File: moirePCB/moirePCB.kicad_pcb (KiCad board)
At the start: 4 copper layers, 38 x 215.8 mm, 57 parts, among them J1 USB_C_Receptacle, U1 ESP32-PICO-D4, U10 TLV73333PDBV, U2 BQ25504, U3 TLV73333PDBV, U4 RFM95W-915S2, U5 CH340E, U6 TLC555xD, U7 HDC1080, U8 AP2281-1WG-7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

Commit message: Daughter Board changes from meeting
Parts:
- removed ACC_RAIL_JP1, BATTMEASURE_JP1, LDO_JP1, TEMP_SCL_JP1, TEMP_SDA_JP1, VBAT_OK1: SolderJumper_2_Bridged, Jumper:SolderJumper-2_P1.3mm_Bridged_RoundedPad1.0x1.5mm
- removed AE1: T1-915M Antenna, Connector_PinHeader_2.54mm:PinHeader_1x01_P2.54mm_Vertical
- removed BOOT1, EN1: SW_Push, Button_Switch_SMD:SW_Push_1P1T_XKB_TS-1187A
- removed BT1: Battery_Cell, Connector_JST:JST_PH_S2B-PH-K_1x02_P2.00mm_Horizontal
- removed C1: .1u, Capacitor_SMD:C_0805_2012Metric
- removed C2, C6: 12pF/50V, Capacitor_SMD:C_0805_2012Metric
- removed C3: .01uF, Capacitor_SMD:C_0805_2012Metric
- removed C5: 10u, Capacitor_SMD:C_0805_2012Metric
- removed C7: 100nF, Capacitor_SMD:C_0805_2012Metric
- removed C_FLTR1: .1uF, Capacitor_SMD:C_0805_2012Metric
- removed C_HVR1, C_STOR1: 4.7uF, Capacitor_SMD:C_0805_2012Metric
- removed LDR1: R_Photo 50k-100k, Connector_PinHeader_2.54mm:PinHeader_1x02_P2.54mm_Horizontal
- removed L_BST1: 22uH, Inductor_SMD:L_0805_2012Metric
- removed R10: 360k, Resistor_SMD:R_0805_2012Metric
- removed R4: 270k, Resistor_SMD:R_0805_2012Metric
- removed R6: 5.1k, Resistor_SMD:R_0805_2012Metric
- removed R7: 820k, Resistor_SMD:R_0805_2012Metric
- removed REF** (x2): MountingHole_3.2mm_M3_DIN965_Pad, MountingHole:MountingHole_3.2mm_M3_DIN965_Pad
- removed R_OC+10: 10M, Resistor_SMD:R_0805_2012Metric
- removed R_OC_1: 5.76M, Resistor_SMD:R_0805_2012Metric
- removed R_OC_2: 4.12M, Resistor_SMD:R_0805_2012Metric
- removed R_OK_1: 3.57M, Resistor_SMD:R_0805_2012Metric
- removed R_OK_2, R_UV_2: 6.19M, Resistor_SMD:R_0805_2012Metric
- removed R_OK_3: .143M, Resistor_SMD:R_0805_2012Metric
- removed R_OV_1: 4.42M, Resistor_SMD:R_0805_2012Metric
- removed R_OV_2: 5.36M, Resistor_SMD:R_0805_2012Metric
- removed R_UV_1: 3.74M, Resistor_SMD:R_0805_2012Metric
- removed SC1: Solar_Cell, Connector_PinHeader_2.54mm:PinHeader_1x02_P2.54mm_Horizontal
- removed U1: ESP32-PICO-D4, Package_DFN_QFN:QFN-48-1EP_7x7mm_P0.5mm_EP5.3x5.3mm
- removed U10, U3: TLV73333PDBV, Package_TO_SOT_SMD:SOT-23-5
- removed U2: BQ25504, Package_DFN_QFN:VQFN-16-1EP_3x3mm_P0.5mm_EP1.68x1.68mm
- removed U4: RFM95W-915S2, RF_Module:HOPERF_RFM9XW_SMD
- removed U5: CH340E, Package_SO:MSOP-10_3x3mm_P0.5mm
- removed U8, U9: AP2281-1WG-7, Package_TO_SOT_SMD:SOT-23-6
- removed USB//OFF1, USB//SOLAR1: SW_DPDT_x2, Button_Switch_SMD:SW_SPDT_PCM12
- removed Y2: 32.768kHz, Crystal:Crystal_SMD_MicroCrystal_CM9V-T1A-2Pin_1.6x1.0mm
- added J2: Conn_01x13, Connector_PinHeader_2.54mm:PinHeader_1x13_P2.54mm_Vertical, F.Cu at (70.9, 72.1)
- J1: value USB_C_Receptacle -> Conn_01x13; footprint Connector_USB:USB_C_Receptacle_HRO_TYPE-C-31-M-12 -> Connector_PinHeader_2.54mm:PinHeader_1x13_P2.54mm_Vertical
- moved U7 60.8 mm to (70.6, 109.7)
- moved J1 45.1 mm to (38.5, 72.2), turned to 0 degrees
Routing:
- net VCC: track 141.9 -> 0.00 mm, vias 7 -> 0
- net A_VCC: track 164.7 -> 48.8 mm
- net Net-(BT1-+): track 107.4 -> 0.00 mm, vias 2 -> 0
- net Net-(SC1-+): track 105.1 -> 0.00 mm, vias 2 -> 0
- net FREQOUT: track 97.2 -> 0.00 mm, vias 2 -> 0
- net /USB5V: track 84.1 -> 0.00 mm, vias 3 -> 0
- net ACCESSORY_SW: track 82.3 -> 0.00 mm, vias 3 -> 0
- net GND: track 354.2 -> 278.6 mm, vias 27 -> 8
- net LDR_MEASURE: track 40.4 -> 0.00 mm, vias 2 -> 0
- net Net-(U2-VIN_DC): track 39.8 -> 0.00 mm, vias 2 -> 0
- net /GPIO_21: track 39.3 -> 0.00 mm
- net Net-(AE1-A): track 35.8 -> 0.00 mm, vias 1 -> 0
- net Net-(U2-VRDIV): track 35.1 -> 0.00 mm, vias 2 -> 0
- net Net-(J2-Pin_5): track 34.7 -> 0.00 mm
- net /D+: track 32.1 -> 0.00 mm
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- removed copper zone on In2.Cu, net GND
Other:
- copper layers 4 -> 2

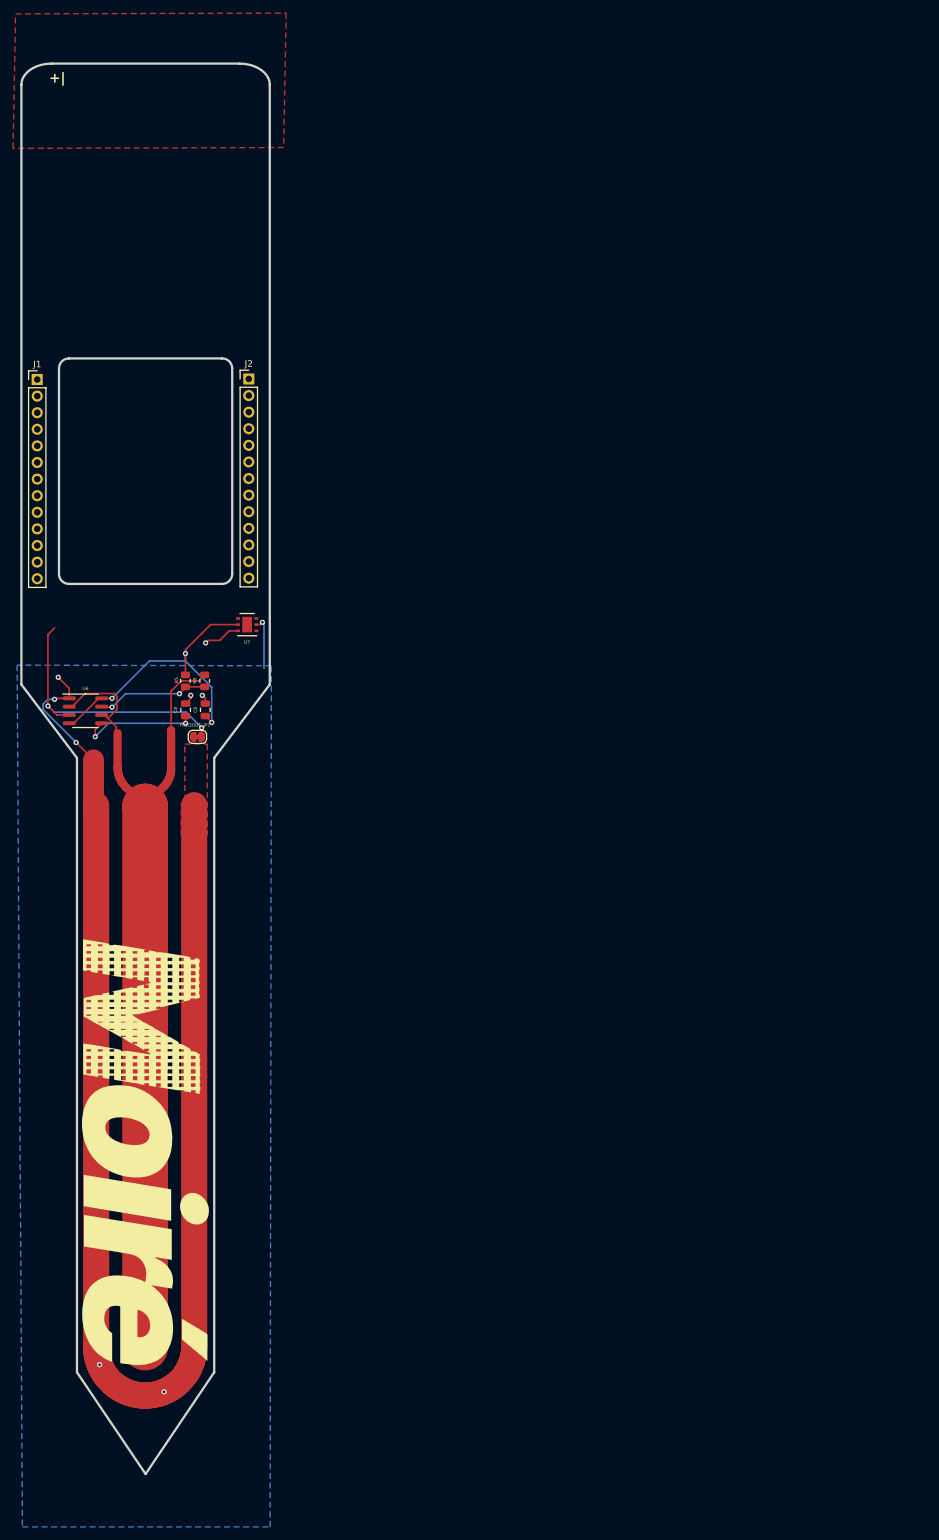
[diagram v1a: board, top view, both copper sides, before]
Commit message: Daughter board prototype 1.0.0
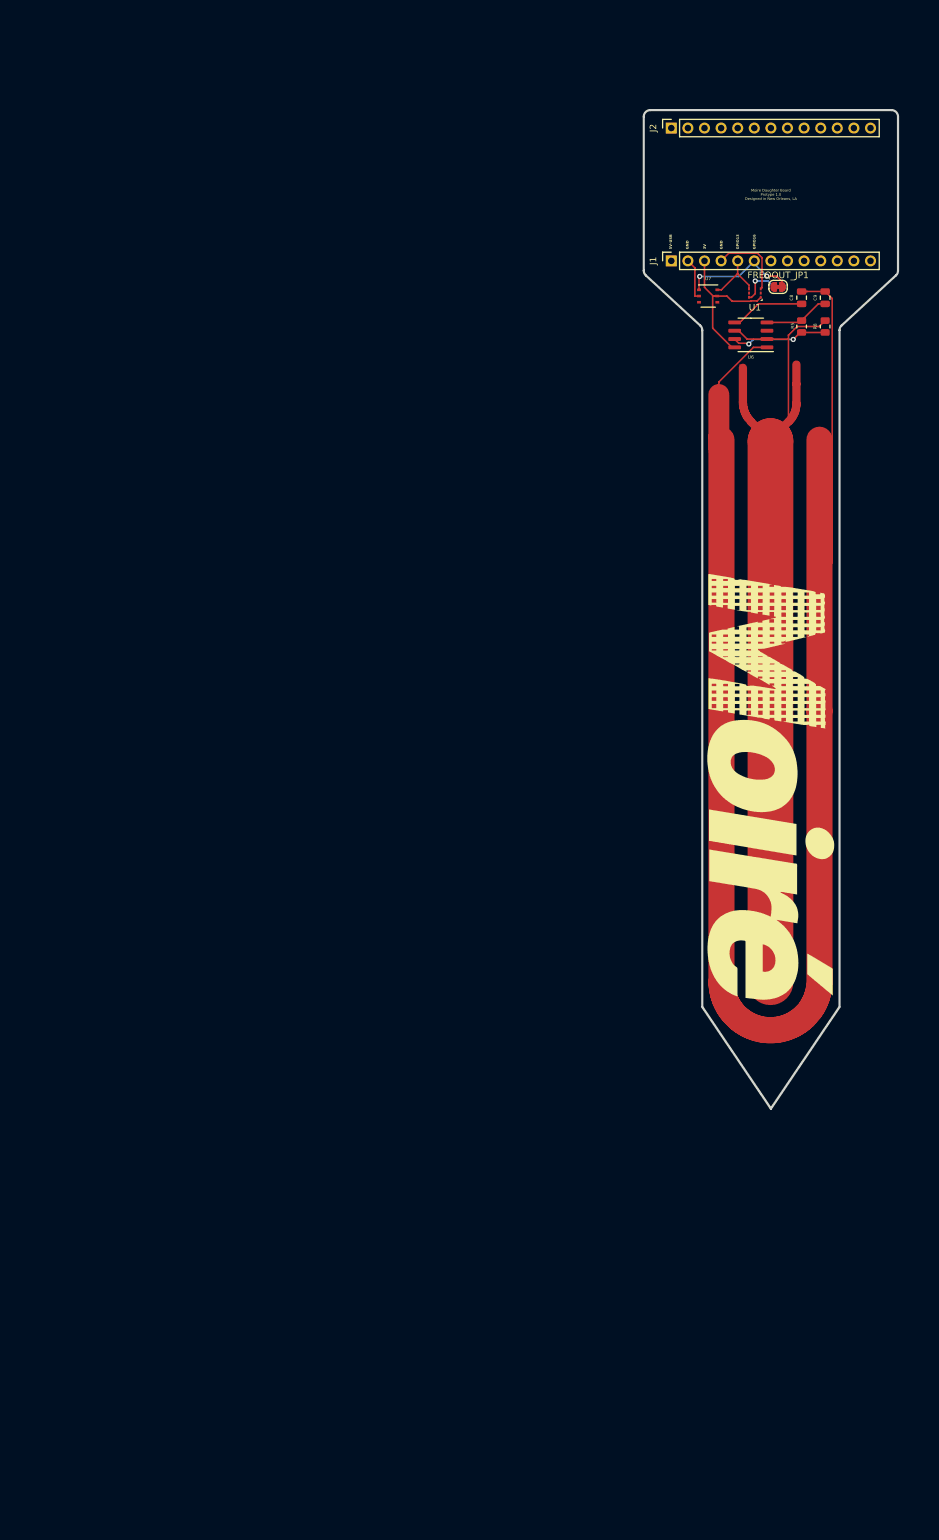
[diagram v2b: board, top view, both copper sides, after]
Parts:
- added U1: OPT3001DNPR, OptTI:OPT3001, F.Cu at (148.3, 59.0)
- J1: value Conn_01x13 -> Conn_01x13 (Right); footprint Connector_PinHeader_2.54mm:PinHeader_1x13_P2.54mm_Vertical -> Connector_PinSocket_2.54mm:PinSocket_1x13_P2.54mm_Vertical
- J2: value Conn_01x13 -> Conn_01x13 (Left); footprint Connector_PinHeader_2.54mm:PinHeader_1x13_P2.54mm_Vertical -> Connector_PinSocket_2.54mm:PinSocket_1x13_P2.54mm_Vertical
- moved U6 116.9 mm to (147.7, 65.4), turned to 180 degrees
- moved C9 113.9 mm to (159.1, 59.7)
- moved J1 113.7 mm to (150.8, 54.1), turned to 90 degrees
- moved C8 113.4 mm to (155.4, 59.7)
- moved FREQOUT_JP1 112.4 mm to (151.8, 58.0)
- moved R8 109.3 mm to (159.1, 64.1)
- moved R5 108.8 mm to (155.4, 64.1)
- moved J2 88.6 mm to (150.8, 33.8), turned to 90 degrees
- moved U7 86.6 mm to (141.2, 59.5), turned to 0 degrees
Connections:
- C9 pad 1: A_VCC -> Net-(U6-R)
- FREQOUT_JP1 pad 1: FREQOUT -> SDA
- FREQOUT_JP1 pad 2: Net-(FREQOUT_JP1-B) -> unconnected-(J1-GPIO16-Pad6)
- J1 pad 1: /5V (USB) -> unconnected-(J1-5V(USB)-Pad1)
- J1 pad 2: GND -> unconnected-(J1-GND-Pad2)
- J1 pad 6: unconnected-(J1-Pin_6-Pad6) -> unconnected-(J1-GPIO16-Pad6)
- J2 pad 1: A_VCC -> VCC
- J2 pad 4: Net-(J2-Pin_4) -> unconnected-(J2-GPIO7(SDC)-Pad4)
- J2 pad 5: Net-(J2-Pin_5) -> FREQOUT
- R5 pad 2: A_VCC -> Net-(U6-R)
- U6 pad 4: A_VCC -> Net-(U6-R)
- U6 pad 8: A_VCC -> Net-(U6-R)
- U7 pad 1: Net-(J2-Pin_5) -> SDA
- U7 pad 5: A_VCC -> VCC
- U7 pad 6: Net-(J2-Pin_4) -> SCL
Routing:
- net GND: track 278.6 -> 328.7 mm, vias 8 -> 0
- net A_VCC: track 48.8 -> 0.00 mm, vias 3 -> 0
- net Net-(FREQOUT_JP1-B): track 42.5 -> 0.00 mm, vias 2 -> 0
- net VCC: track 0.00 -> 23.3 mm
- net SDA: track 0.00 -> 17.6 mm, vias 0 -> 2
- net Net-(U6-R): track 0.00 -> 10.1 mm
- net SCL: track 0.00 -> 9.12 mm
- net Net-(U6-CV): track 18.2 -> 11.4 mm, vias 2 -> 0
- net unconnected-(J1-GPIO16-Pad6): track 0.00 -> 6.36 mm, vias 0 -> 1
- net Net-(J2-Pin_4): track 5.71 -> 0.00 mm, vias 1 -> 0
- net Net-(U6-DIS): track 17.3 -> 16.2 mm
- removed copper zone on B.Cu, net GND
- removed copper zone on F.Cu, net GND
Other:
- board size 38 x 215.8 mm -> 38.9 x 152.8 mm
- board text added: "3V"
- board text added: "5V-USB"
- board text added: "GND"
- board text added: "GPIO13"
- board text added: "GPIO16"
- board text added: "Moire Daughter Board Protype 1.0 Designed in New Orleans, LA"
- board text removed: "+|"

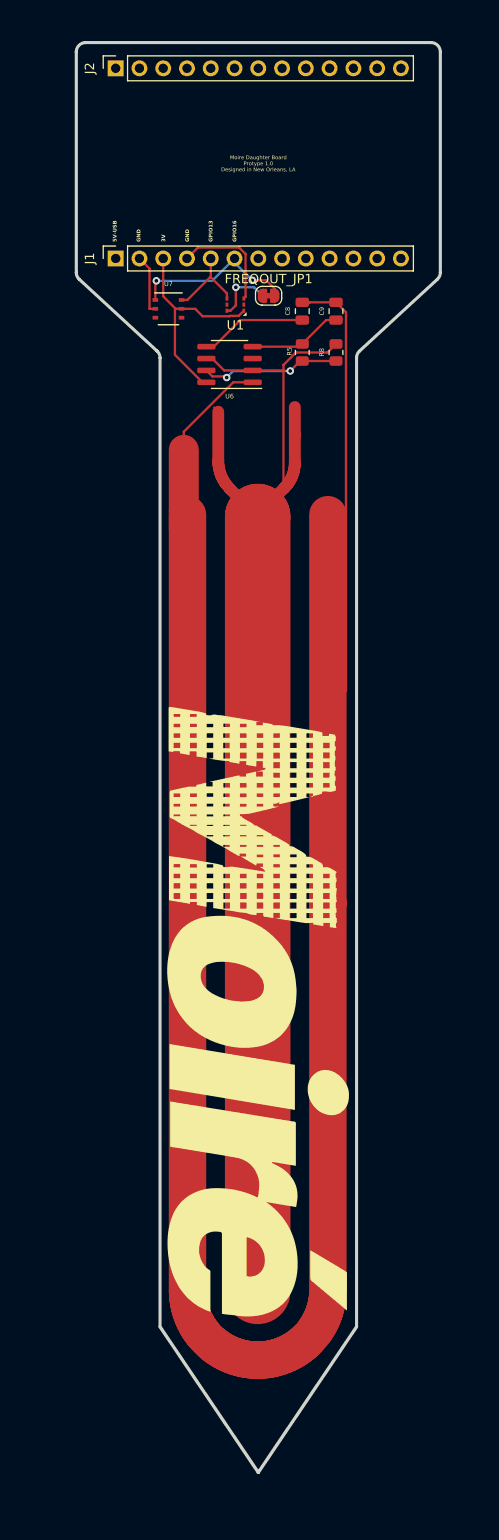
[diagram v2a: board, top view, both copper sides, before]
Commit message: Daughter board prototype 1.0.0
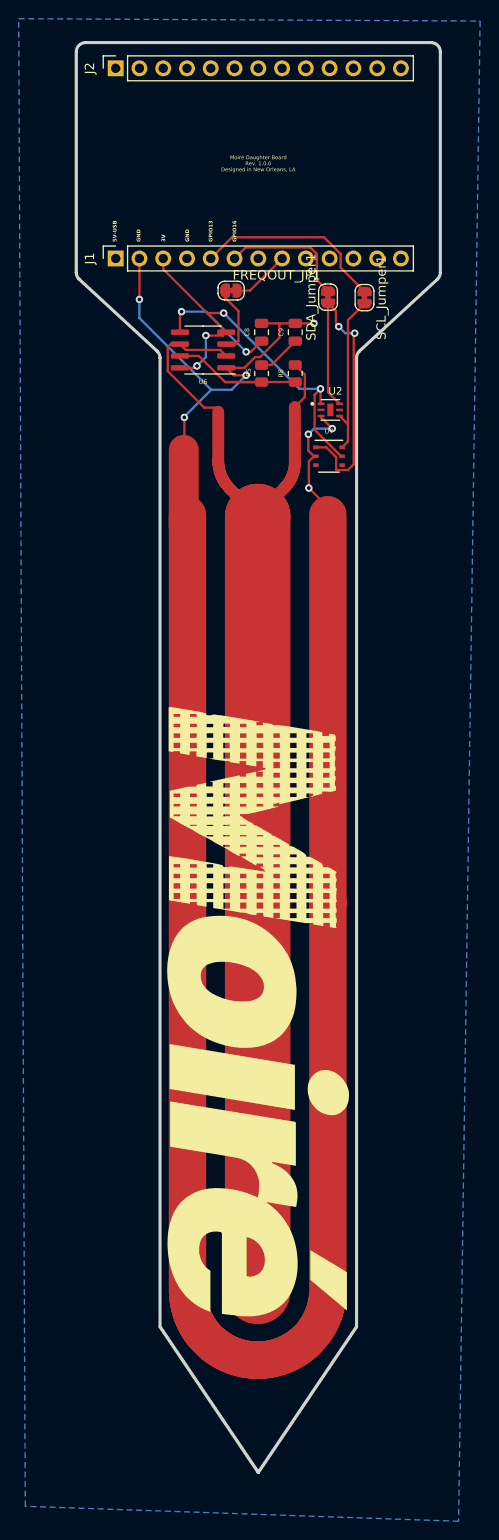
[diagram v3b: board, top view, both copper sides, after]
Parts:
- removed U1: OPT3001DNPR, OptTI:OPT3001
- added SCL_Jumper1: SolderJumper_2_Bridged, Jumper:SolderJumper-2_P1.3mm_Bridged_RoundedPad1.0x1.5mm, F.Cu at (162.1, 58.2)
- added SDA_Jumper1: SolderJumper_2_Bridged, Jumper:SolderJumper-2_P1.3mm_Bridged_RoundedPad1.0x1.5mm, F.Cu at (158.2, 58.2)
- added U2: OPT3001DNPR, OPT3001DNPR:SON65P200X200X65-7N, F.Cu at (158.4, 70.2)
- moved U7 23.3 mm to (158.3, 75.2)
- moved C9 4.90 mm to (154.7, 62.0)
- moved R8 4.90 mm to (154.7, 66.4)
- moved C8 4.90 mm to (151.1, 62.0)
- moved R5 4.90 mm to (151.1, 66.4)
- moved FREQOUT_JP1 4.04 mm to (147.8, 57.5), turned to 180 degrees
- moved U6 3.22 mm to (144.8, 63.9)
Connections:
- C9 pad 1: Net-(U6-R) -> VCC
- FREQOUT_JP1 pad 1: SDA -> FREQOUT_PIN
- FREQOUT_JP1 pad 2: unconnected-(J1-GPIO16-Pad6) -> Net-(FREQOUT_JP1-B)
- J1 pad 2: unconnected-(J1-GND-Pad2) -> GND
- J1 pad 3: unconnected-(J1-3V3-Pad3) -> VCC
- J1 pad 5: unconnected-(J1-GPIO13-Pad5) -> SCL_PIN
- J1 pad 6: unconnected-(J1-GPIO16-Pad6) -> SDA_PIN
- J1 pad 8: unconnected-(J1-GPIO33-Pad8) -> FREQOUT_PIN
- J2 pad 1: VCC -> unconnected-(J2-3V3-Pad1)
- J2 pad 2: GND -> unconnected-(J2-GND-Pad2)
- J2 pad 5: FREQOUT -> unconnected-(J2-GPIO44-Pad5)
- R5 pad 2: Net-(U6-R) -> VCC
- U6 pad 4: Net-(U6-R) -> VCC
- U6 pad 8: Net-(U6-R) -> VCC
- U7 pad 1: SDA -> Net-(SDA_Jumper1-A)
- U7 pad 6: SCL -> Net-(SCL_Jumper1-B)
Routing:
- net Net-(SDA_Jumper1-A): track 0.00 -> 36.4 mm, vias 0 -> 2
- net VCC: track 23.3 -> 49.0 mm, vias 0 -> 4
- net GND: track 328.7 -> 307.9 mm, vias 0 -> 7
- net SCL_PIN: track 0.00 -> 20.6 mm
- net SDA: track 17.6 -> 0.00 mm, vias 2 -> 0
- net Net-(SCL_Jumper1-B): track 0.00 -> 17.6 mm
- net SDA_PIN: track 0.00 -> 14.0 mm
- net Net-(U6-R): track 10.1 -> 0.00 mm
- net SCL: track 9.12 -> 0.00 mm
- net Net-(FREQOUT_JP1-B): track 0.00 -> 7.42 mm
- net PROBE: track 138.6 -> 131.5 mm
- net unconnected-(J1-GPIO16-Pad6): track 6.36 -> 0.00 mm, vias 1 -> 0
- net FREQOUT_PIN: track 0.00 -> 6.21 mm
- net Net-(U6-CV): track 11.4 -> 13.1 mm, vias 0 -> 2
- net Net-(U6-DIS): track 16.2 -> 17.4 mm, vias 2 -> 0
- added copper zone on B.Cu, net GND
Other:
- board text added: "Moiré Daughter Board Rev. 1.0.0 Designed in New Orleans, LA"
- board text removed: "Moire Daughter Board Protype 1.0 Designed in New Orleans, LA"

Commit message: Daughter board prototype 1.0.0
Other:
- board text added: "GPIO10"
- board text added: "GPIO33"
- board text added: "GPIO9"
- board text added: "Moiré Daughter Board Version 1.0.0 Designed in New Orleans, LA"
- board text added: "RESET"
- board text added: "SWCLK"
- board text added: "SWDIO"
- board text added: "SWO"
- board text removed: "Moiré Daughter Board Rev. 1.0.0 Designed in New Orleans, LA"
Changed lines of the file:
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@@
 		(sheetfile "moirePCB.kicad_sch")
 		(zone_connect 1)
-		(attr exclude_from_pos_files allow_soldermask_bridges)
+		(attr exclude_from_pos_files exclude_from_bom allow_soldermask_bridges)
 		(net_tie_pad_groups "1, 2")
 		(fp_poly
@@
 			)
 		)
+		(property "LCSC Part #" "C5307339"
+			(at 0 0 0)
+			(unlocked yes)
+			(layer "F.Fab")
+			(hide yes)
+			(effects
+				(font
+					(size 1 1)
+					(thickness 0.15)
+				)
+			)
+		)
 		(property ki_fp_filters "Connector*:*_1x??_*")
 		(sheetname "/")
@@
 			)
 		)
+		(property "LCSC Part #" "C5307339"
+			(at 0 0 0)
+			(unlocked yes)
+			(layer "F.Fab")
+			(hide yes)
+			(effects
+				(font
+					(size 1 1)
+					(thickness 0.15)
+				)
+			)
+		)
 		(property ki_fp_filters "Connector*:*_1x??_*")
 		(sheetname "/")
@@
 		(sheetfile "moirePCB.kicad_sch")
 		(zone_connect 1)
-		(attr exclude_from_pos_files allow_soldermask_bridges)
+		(attr exclude_from_pos_files exclude_from_bom allow_soldermask_bridges)
 		(net_tie_pad_groups "1, 2")
 		(fp_poly
@@
 		(sheetfile "moirePCB.kicad_sch")
 		(zone_connect 1)
-		(attr exclude_from_pos_files allow_soldermask_bridges)
+		(attr exclude_from_pos_files exclude_from_bom allow_soldermask_bridges)
 		(net_tie_pad_groups "1, 2")
 		(fp_poly
@@
 		)
 	)
+	(gr_text "GPIO9"
+		(at 163.7 52.3 90)
+		(layer "F.SilkS")
+		(effects
+			(font
+				(size 0.4 0.4)
+				(thickness 0.08)
+				(bold yes)
+			)
+			(justify left bottom)
+		)
+	)
+	(gr_text "GPIO33"
+		(at 153.5 52.3 90)
+		(layer "F.SilkS")
+		(effects
+			(font
+				(size 0.4 0.4)
+				(thickness 0.08)
+				(bold yes)
+			)
+			(justify left bottom)
+		)
+	)
+	(gr_text "GPIO10"
+		(at 166.25 52.25 90)
+		(layer "F.SilkS")
+		(effects
+			(font
+				(size 0.4 0.4)
+				(thickness 0.08)
+				(bold yes)
+			)
+			(justify left bottom)
+		)
+	)
 	(gr_text "GPIO16\n"
 		(at 148.45 52.3 90)
@@
 		)
 	)
+	(gr_text "SWDIO\n"
+		(at 156.15 52.3 90)
+		(layer "F.SilkS")
+		(effects
+			(font
+				(size 0.4 0.4)
+				(thickness 0.08)
+				(bold yes)
+			)
+			(justify left bottom)
+		)
+	)
 	(gr_text "GPIO13"
 		(at 145.9 52.3 90)
@@
 		)
 	)
+	(gr_text "SWO"
+		(at 161.15 52.3 90)
+		(layer "F.SilkS")
+		(effects
+			(font
+				(size 0.4 0.4)
+				(thickness 0.08)
+				(bold yes)
+			)
+			(justify left bottom)
+		)
+	)
+	(gr_text "RESET\n"
+		(at 151.15 52.3 90)
+		(layer "F.SilkS")
+		(effects
+			(font
+				(size 0.4 0.4)
+				(thickness 0.08)
+				(bold yes)
+			)
+			(justify left bottom)
+		)
+	)
 	(gr_text "3V\n"
 		(at 140.85 52.3 90)
@@
 		)
 	)
-	(gr_text "Moiré Daughter Board\nRev. 1.0.0\nDesigned in New Orleans, LA"
+	(gr_text "SWCLK\n"
+		(at 158.6 52.25 90)
+		(layer "F.SilkS")
+		(effects
+			(font
+				(size 0.4 0.4)
+				(thickness 0.08)
+				(bold yes)
+			)
+			(justify left bottom)
+		)
+	)
+	(gr_text "Moiré Daughter Board\nVersion 1.0.0\nDesigned in New Orleans, LA"
 		(at 150.75 44.8 0)
 		(layer "F.SilkS")

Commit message: Daughter board prototype 1.0.1
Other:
- board text added: "FREQ"
- board text added: "SCL"
- board text added: "SDA"
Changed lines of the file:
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@@
 		)
 		(property "Value" "OPT3001DNPR"
-			(at 7.652 2.008 0)
+			(at -0.95 -5.65 0)
 			(layer "F.Fab")
+			(hide yes)
 			(effects
 				(font
@@
 			(at -4.85 1.65 0)
 			(layer "F.SilkS")
+			(hide yes)
 			(effects
 				(font
@@
 			(at 0 1.68 90)
 			(layer "F.Fab")
+			(hide yes)
 			(effects
 				(font
@@
 			(at 0 1.68 90)
 			(layer "F.Fab")
+			(hide yes)
 			(effects
 				(font
@@
 			(at 0 -18.01 90)
 			(layer "F.SilkS")
+			(hide yes)
 			(effects
 				(font
@@
 			(at 0 -18.01 90)
 			(layer "F.SilkS")
+			(hide yes)
 			(effects
 				(font
@@
 			(at 0 -1.8 90)
 			(layer "F.SilkS")
+			(hide yes)
 			(effects
 				(font
@@
 			(at 0 1.65 90)
 			(layer "F.Fab")
+			(hide yes)
 			(effects
 				(font
@@
 			(at 0 -1.8 90)
 			(layer "F.SilkS")
+			(hide yes)
 			(effects
 				(font
@@
 		)
 		(property "Value" "10k"
-			(at 0 1.65 90)
+			(at 0 1.45 90)
 			(layer "F.Fab")
+			(hide yes)
 			(effects
 				(font
@@
 		)
 	)
+	(gr_text "SCL"
+		(at 163.45 59.15 0)
+		(layer "F.SilkS")
+		(effects
+			(font
+				(size 0.4 0.4)
+				(thickness 0.08)
+				(bold yes)
+			)
+			(justify left bottom)
+		)
+	)
+	(gr_text "SDA\n"
+		(at 155.5 59.1 0)
+		(layer "F.SilkS")
+		(effects
+			(font
+				(size 0.4 0.4)
+				(thickness 0.08)
+				(bold yes)
+			)
+			(justify left bottom)
+		)
+	)
 	(gr_text "GPIO13"
 		(at 145.9 52.3 90)
@@
 		)
 	)
+	(gr_text "FREQ"
+		(at 144.6 57.7 0)
+		(layer "F.SilkS")
+		(effects
+			(font
+				(size 0.4 0.4)
+				(thickness 0.08)
+				(bold yes)
+			)
+			(justify left bottom)
+		)
+	)
 	(gr_text "SWCLK\n"
 		(at 158.6 52.25 90)
@@
 		(effects
 			(font
-				(size 0.4 0.4)
-				(thickness 0.05)
+				(size 0.6 0.6)
+				(thickness 0.08)
 			)
 			(justify bottom)
@@
 		(min_thickness 0.25)
 		(filled_areas_thickness no)
-		(fill
+		(fill yes
 			(thermal_gap 0.5)
 			(thermal_bridge_width 0.5)
